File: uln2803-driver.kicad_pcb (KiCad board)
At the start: 2 copper layers, 50 x 50 mm, 15 parts, among them K1 BAT, P1 IN1, P2 IN2, P3 IN3, P4 IN4, P5 OUT1, P6 OUT2, P7 OUT3, P8 OUT4, U1 ULN2803

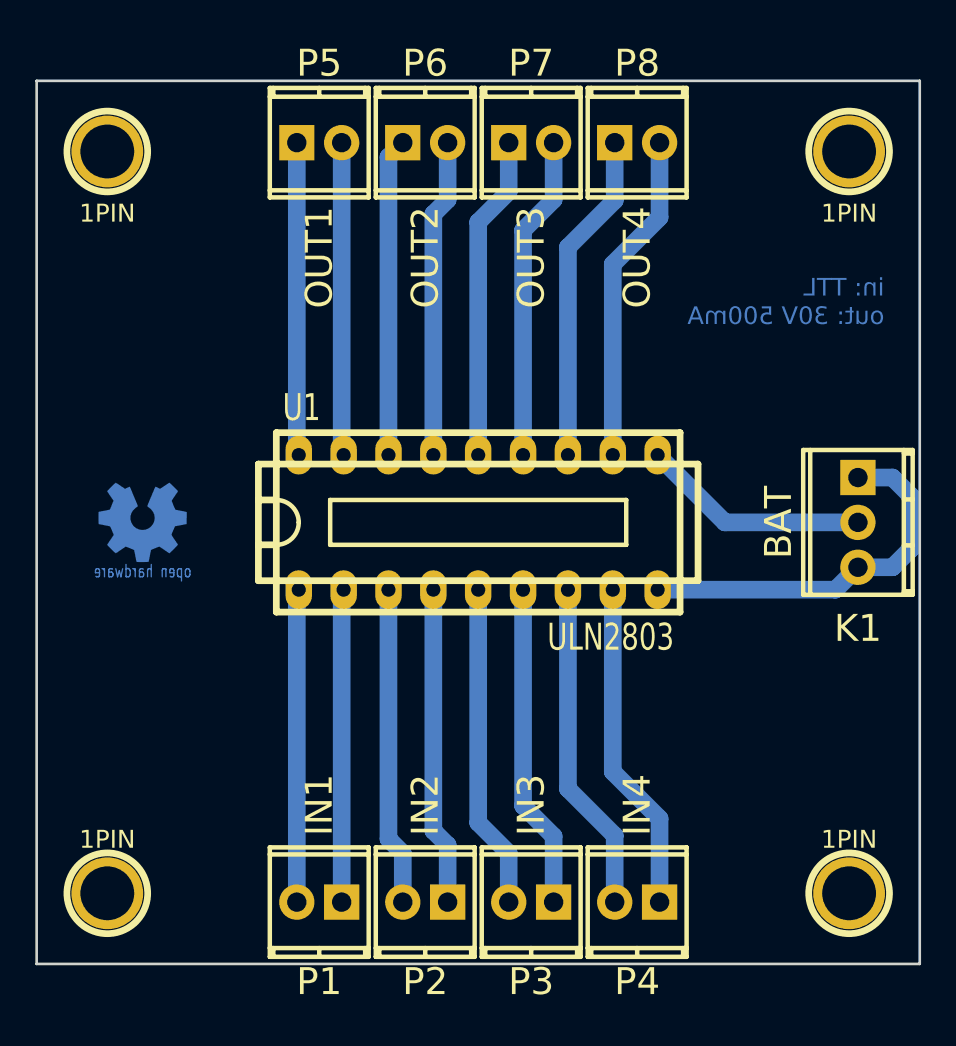
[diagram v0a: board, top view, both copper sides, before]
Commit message: Changed borniers from mpt with 2,54mm pitch to mkds with 5mm pitch. Added filled zones to connect GND.
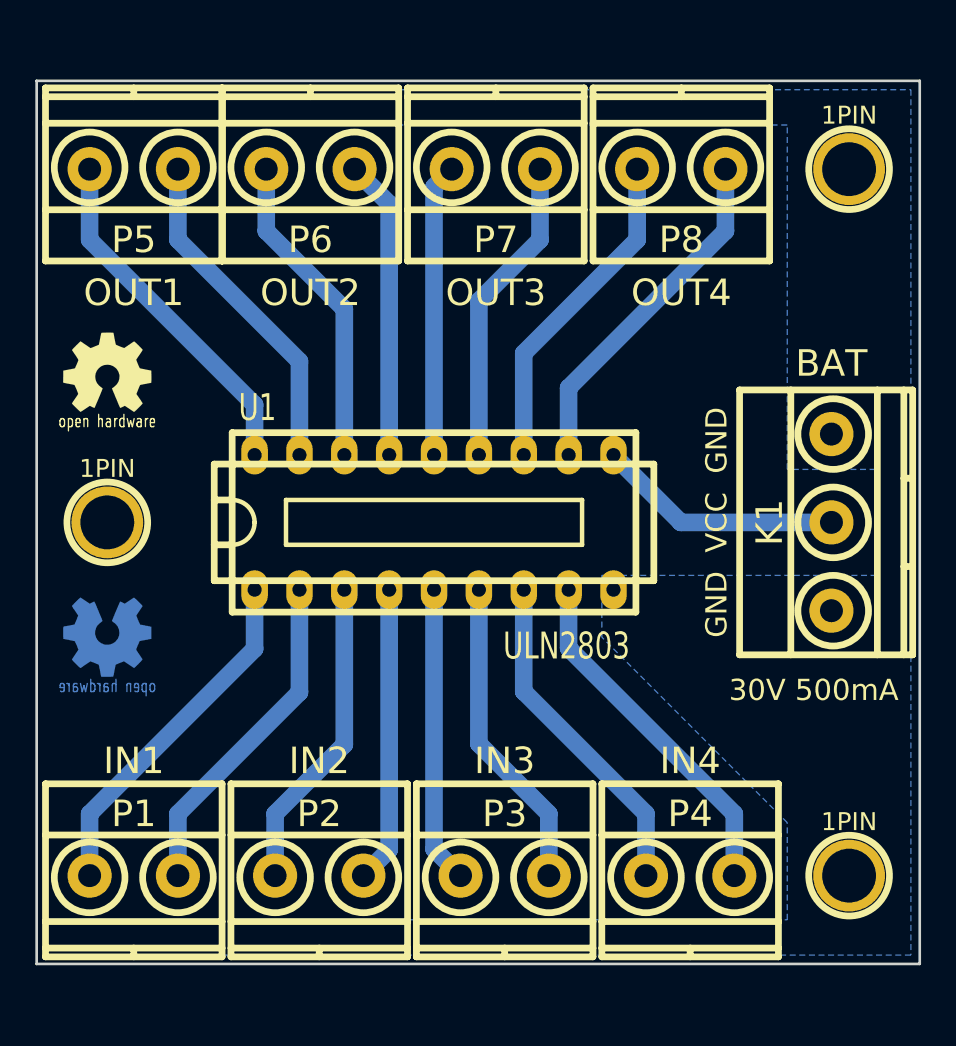
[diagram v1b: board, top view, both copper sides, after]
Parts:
- removed the 1PIN at (124.5, 116.5)
- removed the 1PIN at (82.5, 116.5)
- removed the 1PIN at (82.5, 158.5)
- removed the 1PIN at (124.5, 158.5)
- added 1PIN: P***, 1pin, F.Cu at (82.5, 137.5)
- added 1PIN: P***, 1pin, F.Cu at (124.5, 117.5)
- added 1PIN: P***, 1pin, F.Cu at (124.5, 157.5)
- added G***: LOGO, Logo_silk_OSHW_6x6mm, F.Cu at (82.5, 129.0)
- K1: footprint mpt-3-2,54 -> mkds_1,5-3
- P1, P2, P3, P4, P5, P6, P7, P8: footprint mpt-2-2,54 -> mkds_1,5-2
- moved P1 10.6 mm to (84.0, 157.5)
- moved P5 10.6 mm to (84.0, 117.5)
- moved G*** 6.80 mm to (82.5, 144.0)
- moved P6 6.67 mm to (94.0, 117.5)
- moved P2 6.18 mm to (94.5, 157.5)
- moved P4 3.35 mm to (115.5, 157.5)
- moved P8 2.92 mm to (115.0, 117.5)
- moved P7 2.50 mm to (104.5, 117.5)
- moved U1 2.50 mm to (101.0, 137.5)
- moved P3 2.12 mm to (105.0, 157.5)
- moved K1 1.50 mm to (123.5, 137.5)
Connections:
- P1 pad 1: /E1 -> /E0
- P1 pad 2: /E0 -> /E1
- P2 pad 1: /E3 -> /E2
- P2 pad 2: /E2 -> /E3
- P3 pad 1: /E5 -> /E4
- P3 pad 2: /E4 -> /E5
- P4 pad 1: /E7 -> /E6
- P4 pad 2: /E6 -> /E7
- P5 pad 1: /S0 -> /S1
- P5 pad 2: /S1 -> /S0
- P6 pad 1: /S2 -> /S3
- P6 pad 2: /S3 -> /S2
- P7 pad 1: /S4 -> /S5
- P7 pad 2: /S5 -> /S4
- P8 pad 1: /S6 -> /S7
- P8 pad 2: /S7 -> /S6
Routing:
- net GND: track 21.7 -> 0.00 mm
- net /S0: track 17.7 -> 20.1 mm
- net /E0: track 17.7 -> 20.1 mm
- net /S4: track 18.4 -> 16.6 mm
- net /E4: track 18.4 -> 16.8 mm
- net /S1: track 17.7 -> 19.0 mm
- net /E1: track 17.7 -> 19.0 mm
- net /E7: track 18.8 -> 20.1 mm
- net /E3: track 18.0 -> 16.8 mm
- net /S7: track 18.8 -> 19.9 mm
- net /S3: track 18.0 -> 17.0 mm
- net VCC: track 12.9 -> 13.9 mm
- net /S5: track 18.4 -> 17.6 mm
- net /E5: track 18.4 -> 17.8 mm
- added copper zone on B.Cu, net GND
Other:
- board text added: "30V 500mA"
- board text added: "GND VCC GND"
- board text removed: "in: TTL out: 30V 500mA"
